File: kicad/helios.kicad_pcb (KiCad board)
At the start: 4 copper layers, 65 x 56 mm, 83 parts, among them J1 CAN 1 Conn, J14 Serial Breakout, J19 Raspberry_Pi_4, J2 CAN 3 Conn, J22 I2C Breakout, J25 Stemma QT, J26 Stemma QT, J3 CAN 2 Conn, J4 CAN 4 Conn, J5 SWD Programming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

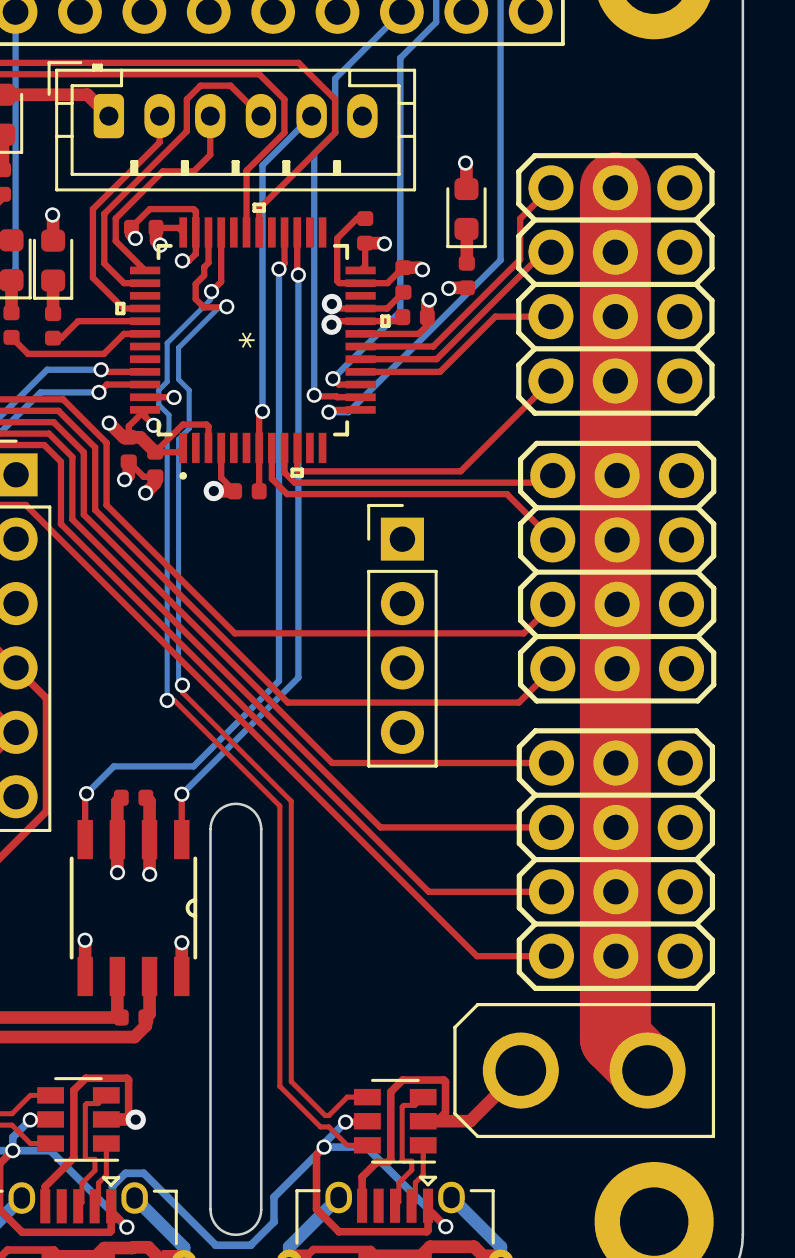
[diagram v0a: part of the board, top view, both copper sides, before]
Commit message: Updated device addressing, added layout picture
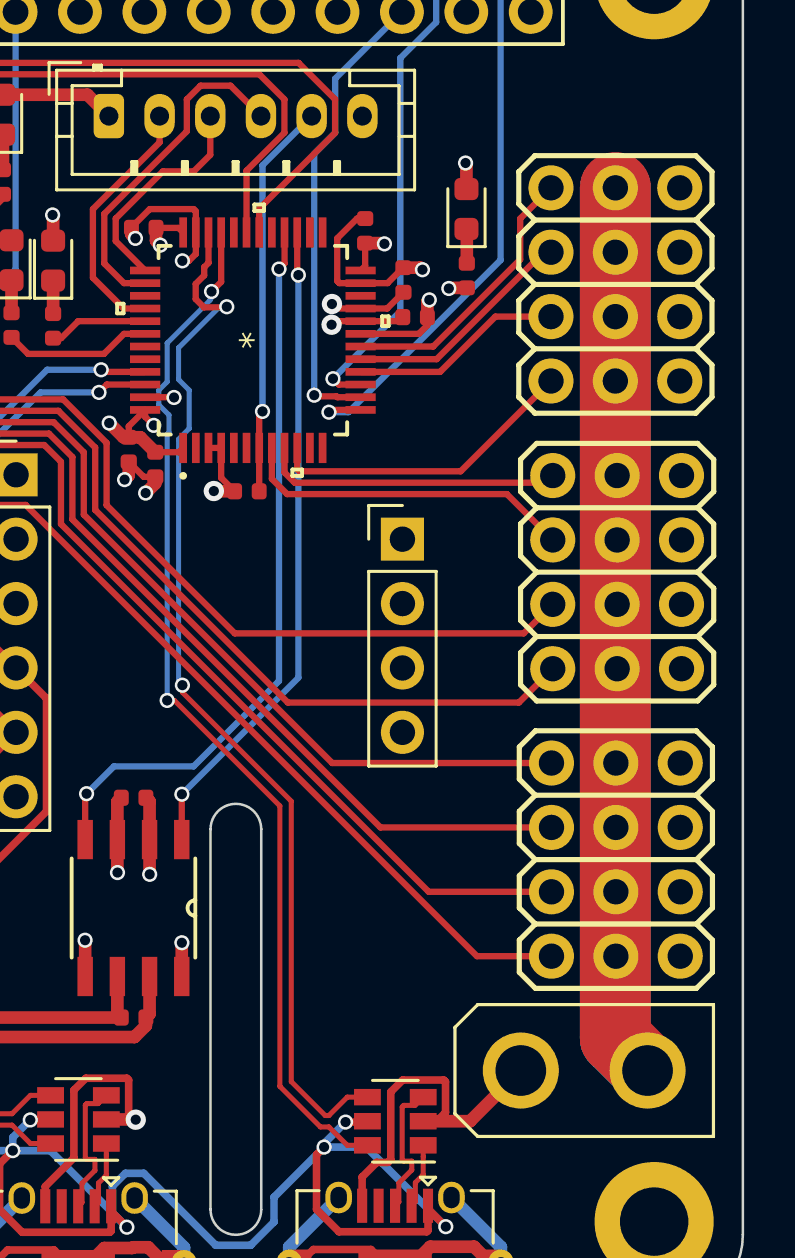
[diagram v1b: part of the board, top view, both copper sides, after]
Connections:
- U6 pad 3: +3V3 -> GND
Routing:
- net +BATT: track 35.3 -> 70.7 mm
- net +3V3: track 62.1 -> 58.7 mm
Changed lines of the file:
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@@
     (thickness 1.6)
     (drawings 35)
-    (tracks 961)
+    (tracks 960)
     (zones 0)
     (modules 83)
@@
   )
   (setup
-    (last_trace_width 0.5)
+    (last_trace_width 0.25)
     (user_trace_width 0.25)
     (user_trace_width 0.3)
@@
     (user_trace_width 1.5)
     (user_trace_width 2)
+    (user_trace_width 2.8)
     (trace_clearance 0.16)
     (zone_clearance 0.508)
@@
       (net 106 "Net-(U6-Pad2)"))
     (pad 3 smd rect (at -4.249999 -1.749999 90) (size 1.1938 0.3048) (layers F.Cu F.Paste F.Mask)
-      (net 2 +3V3))
+      (net 1 GND))
     (pad 4 smd rect (at -4.249999 -1.25 90) (size 1.1938 0.3048) (layers F.Cu F.Paste F.Mask)
       (net 1 GND))
@@
   (gr_line (start 120.34 94.28) (end 120.34 109.28) (layer Edge.Cuts) (width 0.1))
   (gr_line (start 116.34 93.28) (end 119.34 93.28) (layer Edge.Cuts) (width 0.1))
+  (segment (start 175.31 119.02) (end 175.31 85.47) (width 2.8) (layer F.Cu) (net 67))
+  (segment (start 176.58 120.29) (end 175.31 119.02) (width 2.8) (layer F.Cu) (net 67))
   (via (at 126.5 102.39) (size 0.6) (drill 0.4) (layers F.Cu B.Cu) (net 1))
   (segment (start 156.06 122.23) (end 155.23 122.23) (width 0.3) (layer F.Cu) (net 1))
@@
   (segment (start 156.38 122.23) (end 156.39 122.24) (width 0.5) (layer F.Cu) (net 1))
   (segment (start 155.23 122.23) (end 156.38 122.23) (width 0.5) (layer F.Cu) (net 1))
+  (segment (start 159.260001 95.739999) (end 159.76 95.739999) (width 0.25) (layer F.Cu) (net 1))
   (segment (start 144.66 123.09) (end 144.66 124.716) (width 0.5) (layer F.Cu) (net 2))
   (segment (start 143.29 121.72) (end 144.66 123.09) (width 0.5) (layer F.Cu) (net 2))
@@
   (segment (start 158.089999 95.91) (end 158.26 95.739999) (width 0.25) (layer F.Cu) (net 2))
   (segment (start 157.16 95.91) (end 158.089999 95.91) (width 0.25) (layer F.Cu) (net 2))
-  (segment (start 158.251902 94.818098) (end 157.16 95.91) (width 0.25) (layer F.Cu) (net 2))
-  (segment (start 159.185 94.818098) (end 158.251902 94.818098) (width 0.25) (layer F.Cu) (net 2))
-  (segment (start 159.260001 94.893099) (end 159.185 94.818098) (width 0.25) (layer F.Cu) (net 2))
-  (segment (start 159.260001 95.739999) (end 159.260001 94.893099) (width 0.25) (layer F.Cu) (net 2))
   (segment (start 140.241902 94.828098) (end 139.15 95.92) (width 0.25) (layer F.Cu) (net 2))
   (segment (start 141.1724 94.828098) (end 140.241902 94.828098) (width 0.25) (layer F.Cu) (net 2))
@@
   (segment (start 142.30599 118.19599) (end 142.30599 116.479493) (width 0.3) (layer F.Cu) (net 66))
   (segment (start 145.83 121.72) (end 142.30599 118.19599) (width 0.3) (layer F.Cu) (net 66))
-  (segment (start 175.31 119.03) (end 175.31 85.48) (width 2.8) (layer F.Cu) (net 67))
-  (segment (start 176.58 120.3) (end 175.31 119.03) (width 2.8) (layer F.Cu) (net 67))
+  (segment (start 175.31 119.03) (end 175.31 85.48) (width 2.8) (layer B.Cu) (net 67))
+  (segment (start 176.58 120.3) (end 175.31 119.03) (width 2.8) (layer B.Cu) (net 67))
   (segment (start 143.760001 96.596899) (end 143.760001 95.749999) (width 0.25) (layer F.Cu) (net 68))
   (segment (start 143.88001 96.716908) (end 143.760001 96.596899) (width 0.25) (layer F.Cu) (net 68))
